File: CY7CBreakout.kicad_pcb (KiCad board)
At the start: 2 copper layers, 52 x 27.9 mm, 37 parts, among them J1 PORTA, J2 PORTB, J3 PORTD, J4 POWER, J5 WP, J6 +5V Source, U1 CY7C68013A-56LTX, U2 M24128, U3 TLV755P, Y1 24MHz

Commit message: Done some necessary cleanup of the PCB silkscreen to get the right result from running the gerbers
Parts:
- moved LOGO1 0.20 mm to (123.5, 96.5)
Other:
- board text added: "Cypress EZ-USB2 breadboard breakout board"
- board text added: "by Rachel Mant"
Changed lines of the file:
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@@
     (pcbplotparams
       (layerselection 0x010fc_ffffffff)
-      (usegerberextensions false)
-      (usegerberattributes true)
+      (usegerberextensions true)
+      (usegerberattributes false)
       (usegerberadvancedattributes true)
       (creategerberjobfile true)
@@
       (viasonmask false)
       (mode 1)
-      (useauxorigin false)
+      (useauxorigin true)
       (hpglpennumber 1)
       (hpglpenspeed 20)
@@
       (outputformat 1)
       (mirror false)
-      (drillshape 1)
+      (drillshape 0)
       (scaleselection 1)
-      (outputdirectory ""))
+      (outputdirectory "gerber/KiCAD/"))
   )
   (net 0 "")
@@
       (effects (font (size 1 1) (thickness 0.15)))
     )
-    (fp_line (start -4 4) (end -4 -4) (layer F.Fab) (width 0.1))
+    (fp_line (start 4.62 -4.62) (end -4.62 -4.62) (layer F.CrtYd) (width 0.05))
+    (fp_line (start 4.62 4.62) (end 4.62 -4.62) (layer F.CrtYd) (width 0.05))
+    (fp_line (start -4.62 4.62) (end 4.62 4.62) (layer F.CrtYd) (width 0.05))
+    (fp_line (start -4.62 -4.62) (end -4.62 4.62) (layer F.CrtYd) (width 0.05))
+    (fp_line (start -4 -3) (end -3 -4) (layer F.Fab) (width 0.1))
+    (fp_line (start -4 4) (end -4 -3) (layer F.Fab) (width 0.1))
     (fp_line (start 4 4) (end -4 4) (layer F.Fab) (width 0.1))
     (fp_line (start 4 -4) (end 4 4) (layer F.Fab) (width 0.1))
-    (fp_line (start -4 -4) (end 4 -4) (layer F.Fab) (width 0.1))
-    (fp_circle (center -4.3 -3.8) (end -4.2 -3.8) (layer F.SilkS) (width 0.2))
+    (fp_line (start -3 -4) (end 4 -4) (layer F.Fab) (width 0.1))
+    (fp_line (start -3.635 -4.11) (end -4.11 -4.11) (layer F.SilkS) (width 0.12))
+    (fp_line (start 4.11 4.11) (end 4.11 3.635) (layer F.SilkS) (width 0.12))
+    (fp_line (start 3.635 4.11) (end 4.11 4.11) (layer F.SilkS) (width 0.12))
+    (fp_line (start -4.11 4.11) (end -4.11 3.635) (layer F.SilkS) (width 0.12))
+    (fp_line (start -3.635 4.11) (end -4.11 4.11) (layer F.SilkS) (width 0.12))
+    (fp_line (start 4.11 -4.11) (end 4.11 -3.635) (layer F.SilkS) (width 0.12))
+    (fp_line (start 3.635 -4.11) (end 4.11 -4.11) (layer F.SilkS) (width 0.12))
     (pad 1 smd roundrect (at -4.0375 -3.25) (size 0.875 0.25) (layers F.Cu F.Paste F.Mask) (roundrect_rratio 0.25)
       (net 14 "Net-(U1-Pad1)"))
@@
   )
   (module Symbol:OSHW-Logo2_7.3x6mm_SilkScreen (layer F.Cu)
-    (at 123.5 96.7)
+    (at 123.5 96.5)
     (descr "Open Source Hardware Symbol")
     (tags "Logo Symbol OSHW")
@@
     )
   )
-  (module Connector_PinHeader_2.54mm:PinHeader_1x02_P2.54mm_Vertical (layer F.Cu)
+  (module Connector_PinHeader_2.54mm:PinHeader_1x02_P2.54mm_Vertical locked (layer F.Cu)
     (at 164.45 97.5 270)
     (descr "Through hole straight pin header, 1x02, 2.54mm pitch, single row")
@@
       (effects (font (size 1 1) (thickness 0.15)))
     )
-    (fp_text value "+5V Source" (at 2.2 1.25 180) (layer F.Fab)
+    (fp_text value "+5V Source" (at 2.2 1.25 180) (layer F.SilkS)
       (effects (font (size 1 1) (thickness 0.15)))
     )
@@
     )
   )
-  (module Connector_PinHeader_2.54mm:PinHeader_1x08_P2.54mm_Vertical (layer B.Cu)
+  (module Connector_PinHeader_2.54mm:PinHeader_1x08_P2.54mm_Vertical locked (layer B.Cu)
     (at 145 94.6 90)
     (descr "Through hole straight pin header, 1x08, 2.54mm pitch, single row")
@@
       (effects (font (size 1 1) (thickness 0.15)) (justify left mirror))
     )
-    (fp_text value PORTD (at -2.2 -19.2) (layer B.Fab)
+    (fp_text value PORTD (at -2.2 -19.2) (layer B.SilkS)
       (effects (font (size 1 1) (thickness 0.15)) (justify right mirror))
     )
@@
     (at 133.6 101.3 180)
     (attr smd)
-    (fp_text reference Y1 (at 0 1.697056) (layer F.SilkS)
+    (fp_text reference Y1 (at 1.9 0 90) (layer F.SilkS)
       (effects (font (size 1 1) (thickness 0.1)) (justify bottom))
     )
@@
       (effects (font (size 1 1) (thickness 0.15)))
     )
-    (fp_text value WP (at 2.06 2.93 180) (layer F.Fab)
+    (fp_text value WP (at 2.06 2.93 180) (layer F.SilkS)
       (effects (font (size 1 1) (thickness 0.15)))
     )
@@
     )
   )
-  (module Connector_PinHeader_2.54mm:PinHeader_1x08_P2.54mm_Vertical (layer B.Cu)
+  (module Connector_PinHeader_2.54mm:PinHeader_1x08_P2.54mm_Vertical locked (layer B.Cu)
     (at 169.53 94.6 90)
     (descr "Through hole straight pin header, 1x08, 2.54mm pitch, single row")
@@
       (effects (font (size 1 1) (thickness 0.15)) (justify left mirror))
     )
-    (fp_text value POWER (at -2.2 -19.33) (layer B.Fab)
+    (fp_text value POWER (at -2.2 -19.33) (layer B.SilkS)
       (effects (font (size 1 1) (thickness 0.15)) (justify right mirror))
     )
@@
       (effects (font (size 1 1) (thickness 0.15)) (justify left mirror))
     )
-    (fp_text value PORTB (at -2.06 1.35) (layer B.Fab)
+    (fp_text value PORTB (at -2.06 1.35) (layer B.SilkS)
       (effects (font (size 1 1) (thickness 0.15)) (justify right mirror))
     )
@@
       (effects (font (size 1 1) (thickness 0.15)) (justify left mirror))
     )
-    (fp_text value PORTA (at -2.06 1.15) (layer B.Fab)
+    (fp_text value PORTA (at -2.06 1.15) (layer B.SilkS)
       (effects (font (size 1 1) (thickness 0.15)) (justify right mirror))
     )
@@
     )
   )
+  (gr_text "Cypress EZ-USB2 breadboard\nbreakout board" (at 132.3 114.4) (layer F.SilkS)
+    (effects (font (size 1 1) (thickness 0.1)))
+  )
+  (gr_text "by Rachel Mant" (at 128 98) (layer F.SilkS)
+    (effects (font (size 1 1) (thickness 0.1)) (justify left))
+  )
   (gr_poly (pts (xy 131.7 110.3) (xy 131.7 111.7) (xy 130.3 111.7) (xy 130.3 110.3)) (layer B.Mask) (width 0.1))

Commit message: Added some PCB art in the form of Tohru and Nagadreth
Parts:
- added DRG1: トール, トール:トール-12.9x14.8, F.Cu at (158.0, 108.5)
- added DRG2: Nagadreth, Nagadreth:Nagadreth-12.0x12.0, B.Cu at (155.7, 108.6)

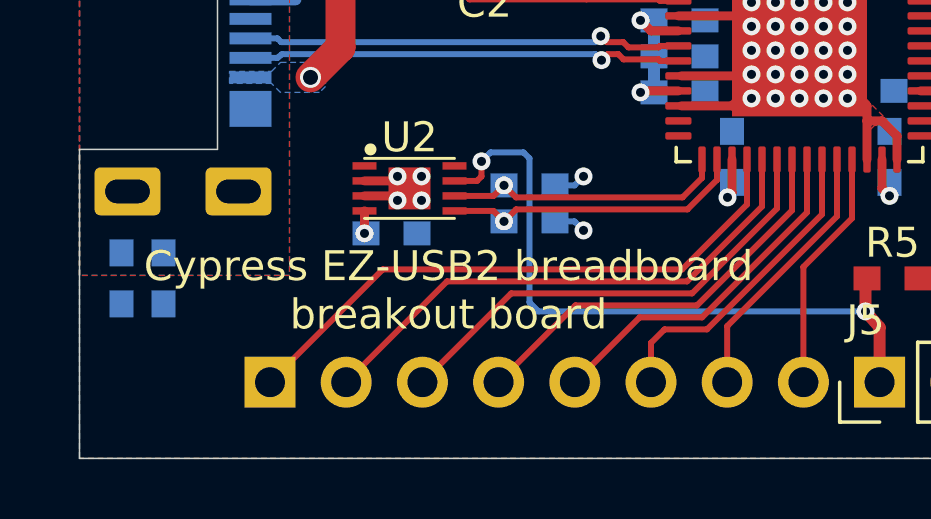
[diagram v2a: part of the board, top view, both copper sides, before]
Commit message: Added a note to the board that this is the first revision, in case additional revisions end up being made
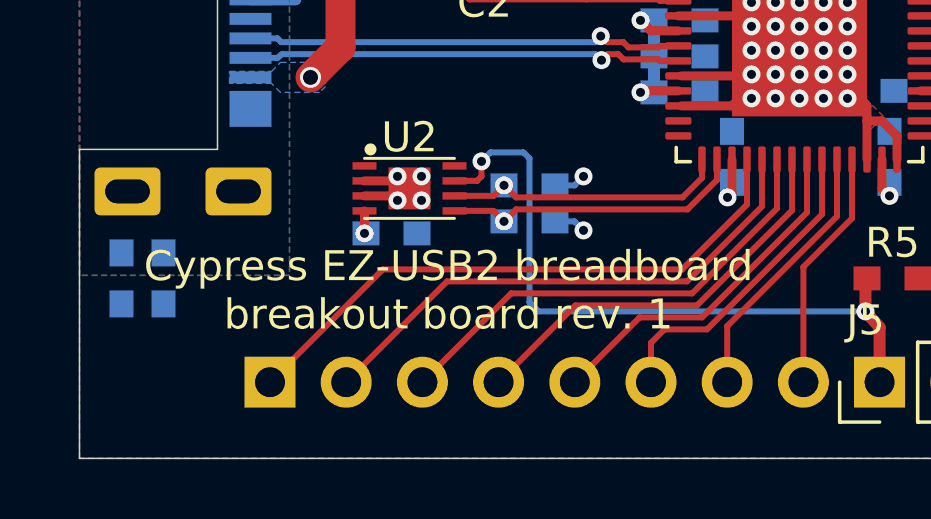
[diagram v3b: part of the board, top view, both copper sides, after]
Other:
- board text added: "Cypress EZ-USB2 breadboard breakout board rev. 1"
- board text removed: "Cypress EZ-USB2 breadboard breakout board"
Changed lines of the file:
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@@
-      (effects (font (size 1 1) (thickness 0.15)))
-    )
-    (fp_text user %R (at 0 0) (layer F.Fab) hide
       (effects (font (size 1 1) (thickness 0.15)))
     )
@@
     (fp_line (start 4.11 -4.11) (end 4.11 -3.635) (layer F.SilkS) (width 0.12))
     (fp_line (start 3.635 -4.11) (end 4.11 -4.11) (layer F.SilkS) (width 0.12))
+    (fp_text user %R (at 0 0) (layer F.Fab) hide
+      (effects (font (size 1 1) (thickness 0.15)))
+    )
     (pad 1 smd roundrect (at -4.0375 -3.25) (size 0.875 0.25) (layers F.Cu F.Paste F.Mask) (roundrect_rratio 0.25)
       (net 14 "Net-(U1-Pad1)"))
@@
       (effects (font (size 1 1) (thickness 0.15)))
     )
-    (fp_text user %R (at 0 0 90) (layer F.Fab) hide
-      (effects (font (size 0.5 0.5) (thickness 0.075)))
-    )
     (fp_line (start -1 1) (end -1 -1) (layer F.Fab) (width 0.15))
     (fp_line (start 1 1) (end -1 1) (layer F.Fab) (width 0.15))
@@
     (fp_line (start -1 -1) (end 1 -1) (layer F.Fab) (width 0.15))
     (fp_circle (center -1 -1.1) (end -0.9 -1.1) (layer F.SilkS) (width 0.2))
+    (fp_text user %R (at 0 0 90) (layer F.Fab) hide
+      (effects (font (size 0.5 0.5) (thickness 0.075)))
+    )
     (pad "" smd rect (at 0 0.4 90) (size 0.82 0.63) (layers F.Paste))
     (pad "" smd rect (at 0 -0.4 90) (size 0.82 0.63) (layers F.Paste))
@@
     )
     (fp_text value "+5V Source" (at 2.2 1.25 180) (layer F.SilkS)
-      (effects (font (size 1 1) (thickness 0.15)))
-    )
-    (fp_text user %R (at 0 1.27) (layer F.Fab) hide
       (effects (font (size 1 1) (thickness 0.15)))
     )
@@
     (fp_line (start 1.8 4.35) (end 1.8 -1.8) (layer F.CrtYd) (width 0.05))
     (fp_line (start 1.8 -1.8) (end -1.8 -1.8) (layer F.CrtYd) (width 0.05))
+    (fp_text user %R (at 0 1.27) (layer F.Fab) hide
+      (effects (font (size 1 1) (thickness 0.15)))
+    )
     (pad 2 thru_hole oval (at 0 2.54 270) (size 1.7 1.7) (drill 1) (layers *.Cu *.Mask)
       (net 47 /Processor+USB/VBUS))
@@
     (fp_text value PORTD (at -2.2 -19.2) (layer B.SilkS)
       (effects (font (size 1 1) (thickness 0.15)) (justify right mirror))
-    )
-    (fp_text user %R (at 0 -8.89) (layer B.Fab) hide
-      (effects (font (size 1 1) (thickness 0.15)) (justify mirror))
     )
     (fp_line (start -0.635 1.27) (end 1.27 1.27) (layer B.Fab) (width 0.1))
@@
     (fp_line (start 1.8 -19.55) (end 1.8 1.8) (layer B.CrtYd) (width 0.05))
     (fp_line (start 1.8 1.8) (end -1.8 1.8) (layer B.CrtYd) (width 0.05))
+    (fp_text user %R (at 0 -8.89) (layer B.Fab) hide
+      (effects (font (size 1 1) (thickness 0.15)) (justify mirror))
+    )
     (pad 8 thru_hole oval (at 0 -17.78 90) (size 1.7 1.7) (drill 1) (layers *.Cu *.Mask)
       (net 33 "/Breadboard Connectors/PD7"))
@@
       (effects (font (size 1 1) (thickness 0.15)))
     )
-    (fp_text user %R (at 0 1.27) (layer F.Fab) hide
-      (effects (font (size 1 1) (thickness 0.15)))
-    )
     (fp_line (start -0.635 -1.27) (end 1.27 -1.27) (layer F.Fab) (width 0.1))
     (fp_line (start 1.27 -1.27) (end 1.27 3.81) (layer F.Fab) (width 0.1))
@@
     (fp_line (start 1.8 4.35) (end 1.8 -1.8) (layer F.CrtYd) (width 0.05))
     (fp_line (start 1.8 -1.8) (end -1.8 -1.8) (layer F.CrtYd) (width 0.05))
+    (fp_text user %R (at 0 1.27) (layer F.Fab) hide
+      (effects (font (size 1 1) (thickness 0.15)))
+    )
     (pad 2 thru_hole oval (at 0 2.54 90) (size 1.7 1.7) (drill 1) (layers *.Cu *.Mask)
       (net 1 GND))
@@
     (fp_text value POWER (at -2.2 -19.33) (layer B.SilkS)
       (effects (font (size 1 1) (thickness 0.15)) (justify right mirror))
-    )
-    (fp_text user %R (at 0 -8.89) (layer B.Fab) hide
-      (effects (font (size 1 1) (thickness 0.15)) (justify mirror))
     )
     (fp_line (start -0.635 1.27) (end 1.27 1.27) (layer B.Fab) (width 0.1))
@@
     (fp_line (start 1.8 -19.55) (end 1.8 1.8) (layer B.CrtYd) (width 0.05))
     (fp_line (start 1.8 1.8) (end -1.8 1.8) (layer B.CrtYd) (width 0.05))
+    (fp_text user %R (at 0 -8.89) (layer B.Fab) hide
+      (effects (font (size 1 1) (thickness 0.15)) (justify mirror))
+    )
     (pad 8 thru_hole oval (at 0 -17.78 90) (size 1.7 1.7) (drill 1) (layers *.Cu *.Mask)
       (net 2 +3V3))
@@
     (fp_text value PORTB (at -2.06 1.35) (layer B.SilkS)
       (effects (font (size 1 1) (thickness 0.15)) (justify right mirror))
-    )
-    (fp_text user %R (at 0 -8.89) (layer B.Fab) hide
-      (effects (font (size 1 1) (thickness 0.15)) (justify mirror))
     )
     (fp_line (start -0.635 1.27) (end 1.27 1.27) (layer B.Fab) (width 0.1))
@@
     (fp_line (start 1.8 -19.55) (end 1.8 1.8) (layer B.CrtYd) (width 0.05))
     (fp_line (start 1.8 1.8) (end -1.8 1.8) (layer B.CrtYd) (width 0.05))
+    (fp_text user %R (at 0 -8.89) (layer B.Fab) hide
+      (effects (font (size 1 1) (thickness 0.15)) (justify mirror))
+    )
     (pad 8 thru_hole oval (at 0 -17.78 270) (size 1.7 1.7) (drill 1) (layers *.Cu *.Mask)
       (net 25 "/Breadboard Connectors/PB7"))
@@
       (effects (font (size 1 1) (thickness 0.15)) (justify right mirror))
     )
-    (fp_text user %R (at 0 -8.89) (layer B.Fab) hide
-      (effects (font (size 1 1) (thickness 0.15)) (justify mirror))
-    )
     (fp_line (start -0.635 1.27) (end 1.27 1.27) (layer B.Fab) (width 0.1))
     (fp_line (start 1.27 1.27) (end 1.27 -19.05) (layer B.Fab) (width 0.1))
@@
     (fp_line (start 1.8 -19.55) (end 1.8 1.8) (layer B.CrtYd) (width 0.05))
     (fp_line (start 1.8 1.8) (end -1.8 1.8) (layer B.CrtYd) (width 0.05))
+    (fp_text user %R (at 0 -8.89) (layer B.Fab) hide
+      (effects (font (size 1 1) (thickness 0.15)) (justify mirror))
+    )
     (pad 8 thru_hole oval (at 0 -17.78 270) (size 1.7 1.7) (drill 1) (layers *.Cu *.Mask)
       (net 17 "/Breadboard Connectors/PA7"))
@@
     )
   )
-  (gr_text "Cypress EZ-USB2 breadboard\nbreakout board" (at 132.3 114.4) (layer F.SilkS)
+  (gr_text "Cypress EZ-USB2 breadboard\nbreakout board rev. 1" (at 132.3 114.4) (layer F.SilkS)
     (effects (font (size 1 1) (thickness 0.1)))
   )
